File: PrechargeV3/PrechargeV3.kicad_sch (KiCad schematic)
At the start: 54 parts, among them J1 430450428, J2 430450428, J4 436500228, Q1 DMN3404L-7, Q2 DMN3404L-7, U1 AMC1351DWVR, U2 AMC1351DWVR, U3 TLV9002QDKRQ1, U4 NMV1S0505SC, U5 NMV1S0505SC

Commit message: Started Layout
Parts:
- removed CR1, CR2: B240A-13-F, Diodes:SMA_DIO, symbol Diodes:B240A-13-F
- added D1, D2: B240A-13-F, Diodes:SMA_DIO, symbol Diodes:B240A-13-F
- added R20: 0, Resistor_SMD:R_0805_2012Metric, symbol Device:R_US
- added TP1: LV_in, TestPoint:TestPoint_Pad_D1.0mm, symbol Connector:TestPoint
- added TP10: INV_GND, TestPoint:TestPoint_Pad_D1.0mm, symbol Connector:TestPoint
- added TP11: BATT_GND, TestPoint:TestPoint_Pad_D1.0mm, symbol Connector:TestPoint
- added TP12: INV_+5, TestPoint:TestPoint_Pad_D1.0mm, symbol Connector:TestPoint
- added TP13: BATT_+5, TestPoint:TestPoint_Pad_D1.0mm, symbol Connector:TestPoint
- added TP2: GND, TestPoint:TestPoint_Pad_D1.0mm, symbol Connector:TestPoint
- added TP3: 5V, TestPoint:TestPoint_Pad_D1.0mm, symbol Connector:TestPoint
- added TP4: Vinv_LV+, TestPoint:TestPoint_Pad_D1.0mm, symbol Connector:TestPoint
- added TP5: Vinv_LV-, TestPoint:TestPoint_Pad_D1.0mm, symbol Connector:TestPoint
- added TP6: Vbatt_LV+, TestPoint:TestPoint_Pad_D1.0mm, symbol Connector:TestPoint
- added TP7: Vbatt_LV-, TestPoint:TestPoint_Pad_D1.0mm, symbol Connector:TestPoint
- added TP8: Inv_measured, TestPoint:TestPoint_Pad_D1.0mm, symbol Connector:TestPoint
- added TP9: Batt_Measured, TestPoint:TestPoint_Pad_D1.0mm, symbol Connector:TestPoint
- C1, C11, C12, C16, C17: value C324C106K3R5TA -> 10u; footprint 10uF Cap:CAP_C324C_MR_X7R_KEM -> Capacitor_SMD:C_1210_3225Metric
- C10, C6, C7, C9: value K331K15X7RF5TL2 -> 330p; footprint 330pFCap:CAP_K-SERIES_15-L2_VIS -> Capacitor_SMD:C_0603_1608Metric
- C2, C3, C4, C5, C8: value K104K10X7RF5UH5 -> 1u; footprint 1uFCap:K104K10X7RF5UH5_VIS -> Capacitor_SMD:C_0805_2012Metric
- R1, R10, R11, R12, R13, R14, R15, R16, R17, R18, R2, R21, R22, R23, R24, R25, R26, R27, R28, R3, R4, R5, R6, R9: footprint Resistor_SMD:R_0603_1608Metric_Pad0.98x0.95mm_HandSolder -> Resistor_SMD:R_0603_1608Metric
- R7: value R_US -> 1.5k; footprint Resistor_SMD:R_0603_1608Metric_Pad0.98x0.95mm_HandSolder -> Resistor_SMD:R_0603_1608Metric
- R8: value R_US -> 1k; footprint Resistor_SMD:R_0603_1608Metric_Pad0.98x0.95mm_HandSolder -> Resistor_SMD:R_0603_1608Metric
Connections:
- net +5V: now also U4.1 (+VIN), U5.1 (+VIN), R20.1, R20.2, TP3.1; no longer U4.7 (+VOUT), U5.7 (+VOUT)
- net BATT+5: now also U5.7 (+VOUT), TP13.1; no longer U5.1 (+VIN)
- net BATT_GND: now also J2.3, U5.5 (-VOUT), TP11.1; no longer J2.1, U5.2 (-VIN)
- net GND: now also U4.2 (-VIN), U5.2 (-VIN), TP2.1; no longer U4.5 (-VOUT), U5.5 (-VOUT)
- net INV+5: now also U4.7 (+VOUT), TP12.1; no longer U4.1 (+VIN)
- net INV_GND: now also J2.4, U4.5 (-VOUT), TP10.1; no longer J2.2, U4.2 (-VIN)
- net ShutdownIn: now also D1.1, D2.1
- net at R22.1, U2.6 (VOUTN): now also TP7.1
- net at J1.1, Q2.3 (D): now also D2.2
- net at R10.1, U1.7 (VOUTP): now also TP4.1
- net BattMeasured: now reaches C9.2, R24.1, U3.7
- net BattMeasured: now also A1.A4 (A4/SDA), TP9.1; no longer A1.A2
- net at R1.1: now also J2.2; no longer J2.4
- net at R9.1, U1.6 (VOUTN): now also TP5.1
- net at R13.1: now also J2.1; no longer J2.3
- net at J4.2, PS1.1 (+VIN): now also TP1.1
- net at J1.2, Q1.3 (D): now also D1.2
- net InvMeasured: now reaches C7.2, R11.1, U3.1
- net InvMeasured: now also A1.A1, TP8.1; no longer A1.A7
- net at R21.1, U2.7 (VOUTP): now also TP6.1

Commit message: Finished Layout
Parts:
- removed A1: Arduino_Nano_33_IoT_Socket, PCM_arduino-library:Arduino_Nano_33_IoT_Socket, symbol PCM_arduino-library:Arduino_Nano_33_IoT_Socket
- added A1: Arduino_Nano_33_IoT_Socket, MCUs:Arduino_Nano_33_IoT_Socket, symbol MCUs:Arduino_Nano_33_IoT_Socket
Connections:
- net +5V: now also A1.VIN
- net BattMeasured: now also A1.A4 (A4/SDA)
- net GND: now also A1.GND1 (GND), A1.GND2 (GND)
- net InvMeasured: now also A1.A1
- net PrechargeStatus: now also A1.D4
- net SenseSHD: now also A1.D5
- net at R25.1: now also A1.D3
- net at R27.1: now also A1.D9
- new net RX: A1.D10
- new net TX: A1.D2
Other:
- title: RM28 Precharge PCB -> RM29 Precharge PCB
- moved on the sheet: C1, C11, C12, C16, C17, J4, PS1, TP1, TP12, TP13, TP2, TP3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

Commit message: Updated Layout
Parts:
- R1, R13, R14, R15, R16, R17, R18, R2, R3, R4, R5, R6: footprint Resistor_SMD:R_0603_1608Metric -> Capacitor_SMD:C_0805_2012Metric
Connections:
- net +5V: now also A1.5V
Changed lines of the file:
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@@
 	)
 	(junction
+		(at 160.02 115.57)
+		(diameter 0)
+		(color 0 0 0 0)
+	)
+	(junction
 		(at 148.59 102.87)
 		(diameter 0)
@@
 	(wire
 		(pts
+			(xy 160.02 115.57) (xy 165.1 115.57)
+		)
+		(stroke
+			(width 0)
+			(type default)
+		)
+	)
+	(wire
+		(pts
 			(xy 130.81 78.74) (xy 130.81 68.58)
 		)
@@
 	(wire
 		(pts
+			(xy 160.02 115.57) (xy 160.02 139.7)
+		)
+		(stroke
+			(width 0)
+			(type default)
+		)
+	)
+	(wire
+		(pts
 			(xy 146.05 149.86) (xy 160.02 149.86)
 		)
@@
 	(wire
 		(pts
-			(xy 160.02 113.03) (xy 160.02 139.7)
+			(xy 160.02 113.03) (xy 160.02 115.57)
 		)
 		(stroke
@@
 	(wire
 		(pts
-			(xy 35.56 62.23) (xy 35.56 95.25)
+			(xy 34.29 62.23) (xy 34.29 95.25)
 		)
 		(stroke
@@
 	(wire
 		(pts
-			(xy 30.48 95.25) (xy 35.56 95.25)
+			(xy 30.48 95.25) (xy 34.29 95.25)
 		)
 		(stroke
@@
 	(wire
 		(pts
-			(xy 35.56 62.23) (xy 34.29 62.23)
-		)
-		(stroke
-			(width 0)
-			(type default)
-		)
-	)
-	(wire
-		(pts
 			(xy 148.59 68.58) (xy 148.59 81.28)
 		)
@@
 			)
 		)
-		(property "Footprint" "Resistor_SMD:R_0603_1608Metric"
+		(property "Footprint" "Capacitor_SMD:C_0805_2012Metric"
 			(at 71.374 110.236 90)
 			(effects
@@
 			)
 		)
-		(property "Footprint" "Resistor_SMD:R_0603_1608Metric"
+		(property "Footprint" "Capacitor_SMD:C_0805_2012Metric"
 			(at 45.974 61.214 90)
 			(effects
@@
 			)
 		)
-		(property "Footprint" "Resistor_SMD:R_0603_1608Metric"
+		(property "Footprint" "Capacitor_SMD:C_0805_2012Metric"
 			(at 68.834 61.214 90)
 			(effects
@@
 			)
 		)
-		(property "Footprint" "Resistor_SMD:R_0603_1608Metric"
+		(property "Footprint" "Capacitor_SMD:C_0805_2012Metric"
 			(at 68.834 104.394 90)
 			(effects
@@
 			)
 		)
-		(property "Footprint" "Resistor_SMD:R_0603_1608Metric"
+		(property "Footprint" "Capacitor_SMD:C_0805_2012Metric"
 			(at 38.354 61.214 90)
 			(effects
@@
 			)
 		)
-		(property "Footprint" "Resistor_SMD:R_0603_1608Metric"
+		(property "Footprint" "Capacitor_SMD:C_0805_2012Metric"
 			(at 61.214 61.214 90)
 			(effects
@@
 			)
 		)
-		(property "Footprint" "Resistor_SMD:R_0603_1608Metric"
+		(property "Footprint" "Capacitor_SMD:C_0805_2012Metric"
 			(at 53.594 61.214 90)
 			(effects
@@
 			)
 		)
-		(property "Footprint" "Resistor_SMD:R_0603_1608Metric"
+		(property "Footprint" "Capacitor_SMD:C_0805_2012Metric"
 			(at 45.974 104.394 90)
 			(effects
@@
 			)
 		)
-		(property "Footprint" "Resistor_SMD:R_0603_1608Metric"
+		(property "Footprint" "Capacitor_SMD:C_0805_2012Metric"
 			(at 61.214 104.394 90)
 			(effects
@@
 			)
 		)
-		(property "Footprint" "Resistor_SMD:R_0603_1608Metric"
+		(property "Footprint" "Capacitor_SMD:C_0805_2012Metric"
 			(at 38.354 104.394 90)
 			(effects
@@
 			)
 		)
-		(property "Footprint" "Resistor_SMD:R_0603_1608Metric"
+		(property "Footprint" "Capacitor_SMD:C_0805_2012Metric"
 			(at 53.594 104.394 90)
 			(effects
@@
 			)
 		)
-		(property "Footprint" "Resistor_SMD:R_0603_1608Metric"
+		(property "Footprint" "Capacitor_SMD:C_0805_2012Metric"
 			(at 71.374 67.056 90)
 			(effects

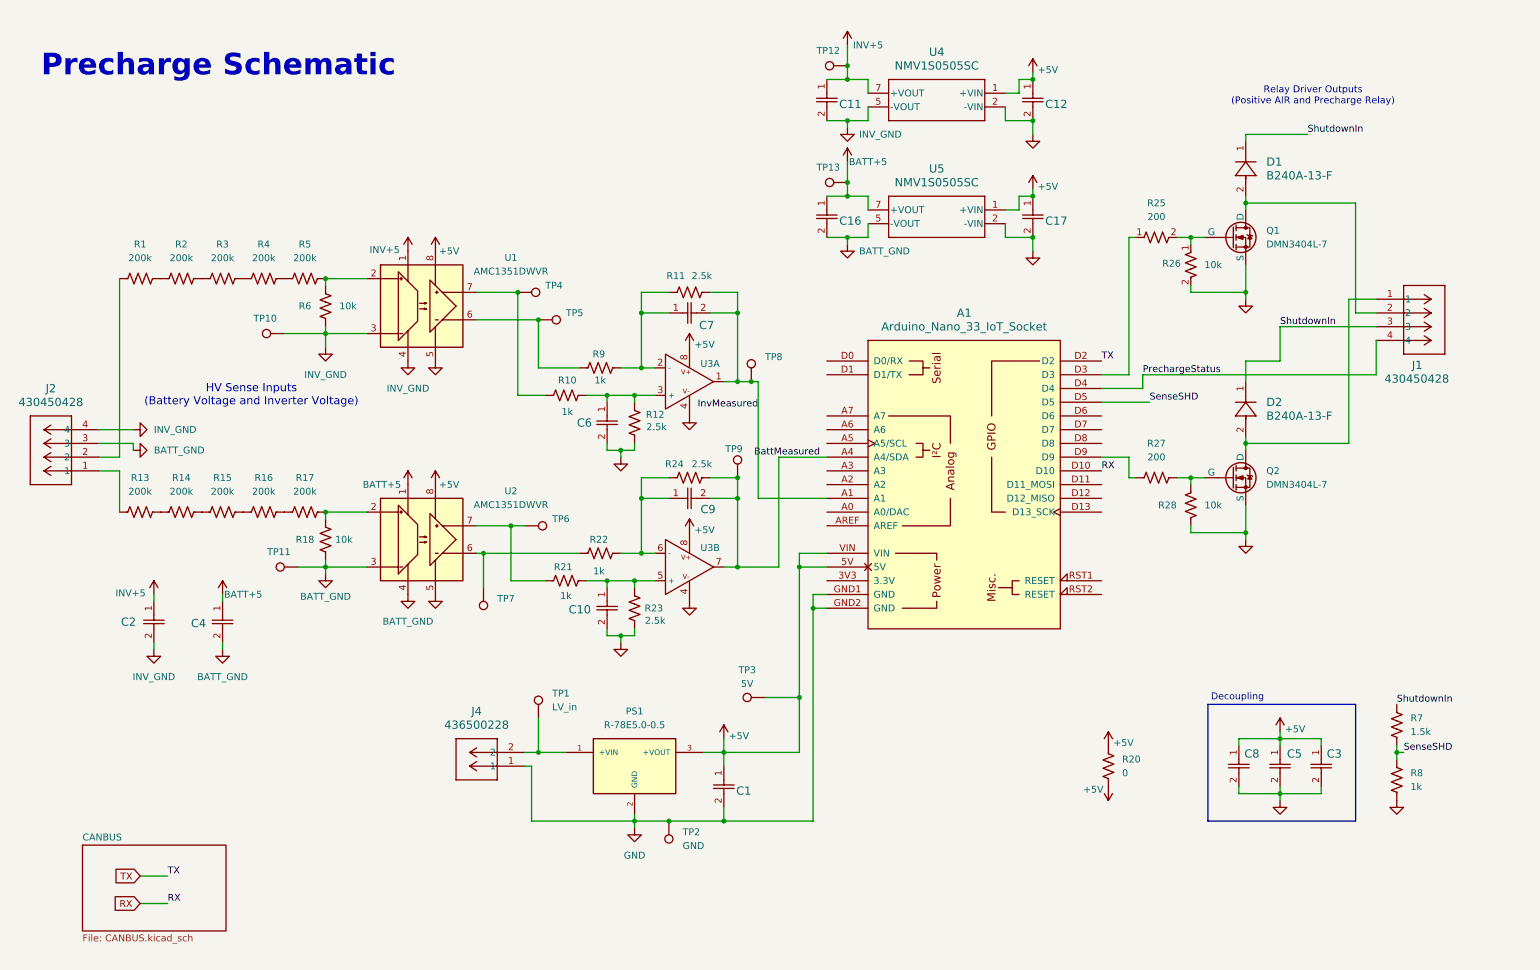
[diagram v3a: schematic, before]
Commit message: Precharge state machine & 3.3v component adjustments
Precharge state machine written for stm32. Differential op-amp and shutdown sense resistor values changed from 5v logic level mcu to 3.3v one.
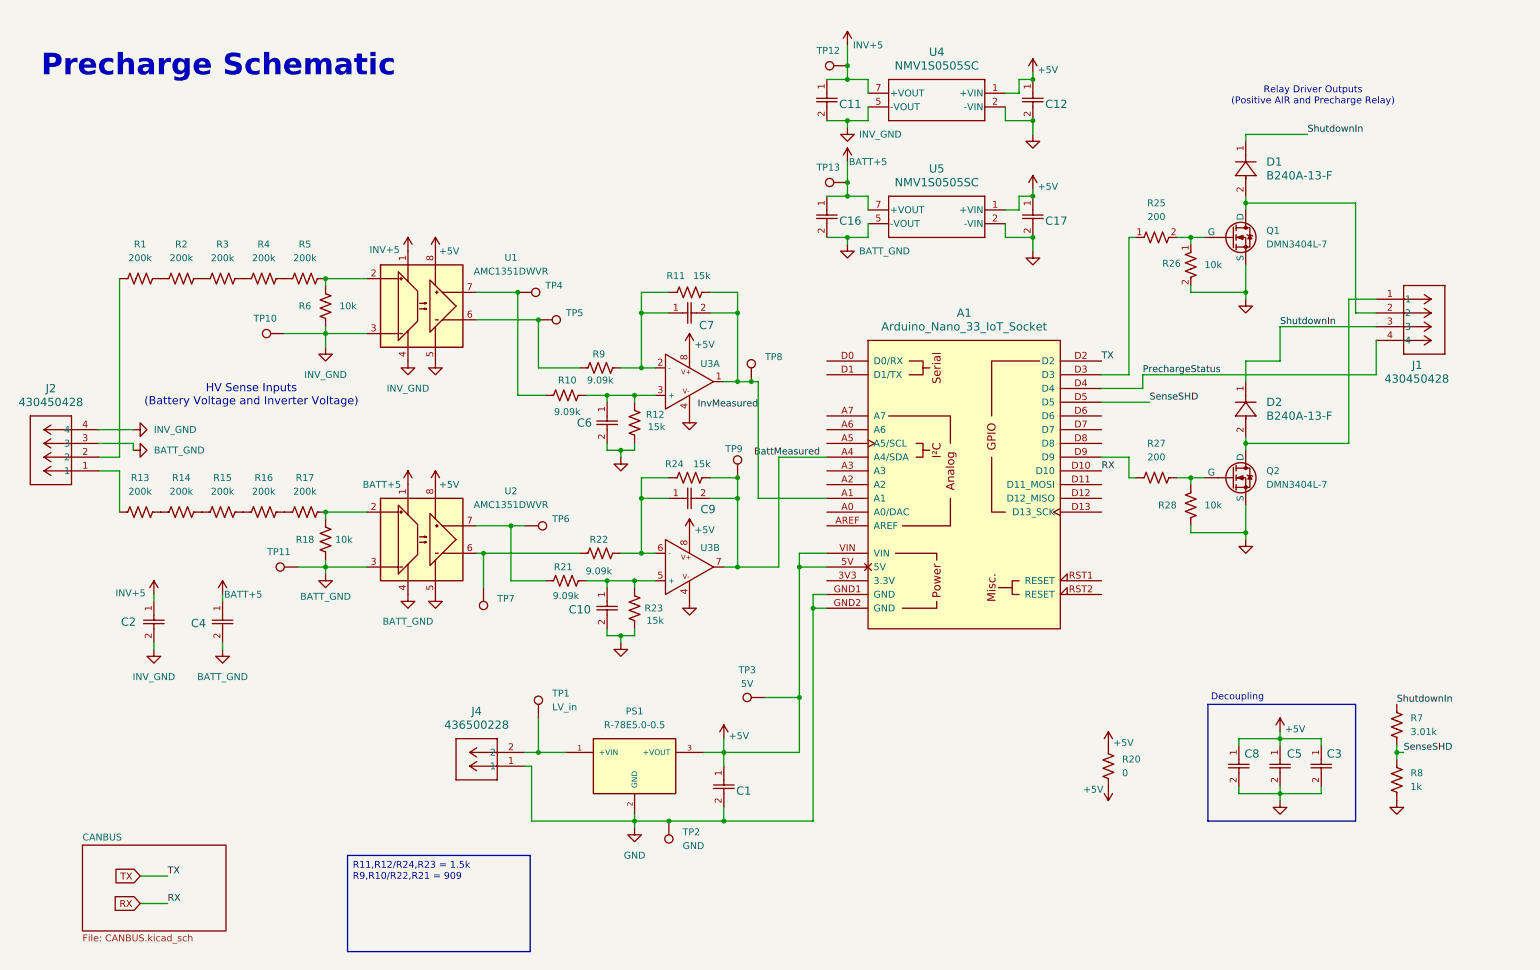
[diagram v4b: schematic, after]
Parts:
- R10, R21, R22, R9: value 1k -> 9.09k
- R11, R12, R23, R24: value 2.5k -> 15k
- R7: value 1.5k -> 3.01k
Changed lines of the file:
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@@
 		)
 	)
+	(text_box "R11,R12/R24,R23 = 1.5k\nR9,R10/R22,R21 = 909\n"
+		(exclude_from_sim no)
+		(at 76.454 168.91 0)
+		(size 33.782 17.78)
+		(margins 0.9525 0.9525 0.9525 0.9525)
+		(stroke
+			(width 0)
+			(type solid)
+		)
+		(fill
+			(type none)
+		)
+		(effects
+			(font
+				(size 1.27 1.27)
+			)
+			(justify left top)
+		)
+	)
 	(junction
 		(at 106.68 107.95)
@@
 			)
 		)
-		(property "Value" "1k"
+		(property "Value" "9.09k"
 			(at 122.936 116.332 90)
 			(effects
@@
 			)
 		)
-		(property "Value" "1k"
+		(property "Value" "9.09k"
 			(at 117.094 86.868 90)
 			(effects
@@
 			)
 		)
-		(property "Value" "1k"
+		(property "Value" "9.09k"
 			(at 123.19 81.026 90)
 			(effects
@@
 			)
 		)
-		(property "Value" "2.5k"
+		(property "Value" "15k"
 			(at 133.604 89.662 0)
 			(effects
@@
 			)
 		)
-		(property "Value" "2.5k"
+		(property "Value" "15k"
 			(at 133.35 125.476 0)
 			(effects
@@
 			)
 		)
-		(property "Value" "1.5k"
+		(property "Value" "3.01k"
 			(at 273.05 146.0499 0)
 			(effects
@@
 			)
 		)
-		(property "Value" "2.5k"
+		(property "Value" "15k"
 			(at 141.986 96.52 90)
 			(effects
@@
 			)
 		)
-		(property "Value" "2.5k"
+		(property "Value" "15k"
 			(at 141.986 61.722 90)
 			(effects
@@
 			)
 		)
-		(property "Value" "1k"
+		(property "Value" "9.09k"
 			(at 116.84 120.904 90)
 			(effects
